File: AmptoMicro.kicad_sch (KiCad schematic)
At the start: 12 parts, among them U1 ADG1207YCPZ-REEL7, U10 ADG1207YCPZ-REEL7, U11 MSP430F6768IPEU, U12 ADL5308ACCZ, U3 ADG1207YCPZ-REEL7, U4 ADG1207YCPZ-REEL7, U5 ADG1207YCPZ-REEL7, U6 ADG1207YCPZ-REEL7, U7 ADG1207YCPZ-REEL7, U8 ADG1207YCPZ-REEL7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

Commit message: With new TMUX
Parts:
- removed U1, U10, U3, U4, U5, U6, U7, U8, U9: ADG1207YCPZ-REEL7, CP_32_2_ADI, symbol ADG_new:ADG1207YCPZ-REEL7
- added U1, U10, U13, U2, U3, U4, U5, U6, U7, U8, U9: TMUX1109PWR, PW_16_TEX, symbol TMUX1109:TMUX1109PWR
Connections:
- net DA1: now also U1.8 (DA), U9.4 (S1A)
- net DA2: now also U2.8 (DA), U9.5 (S2A)
- net DA3: now also U3.8 (DA), U9.6 (S3A)
- net DA4: now also U4.8 (DA), U9.7 (S4A)
- net DA5: now also U13.4 (S1A), U5.8 (DA)
- net DA6: now also U13.5 (S2A), U6.8 (DA)
- net DA7: now also U13.6 (S3A), U7.8 (DA)
- net DA8: now also U13.7 (S4A), U8.8 (DA)
- net DF: now reaches U12.2 (INP)
- net DF: now also U10.8 (DA)
- new net DAA1: U10.4 (S1A), U9.8 (DA)
- new net DAA2: U10.5 (S2A), U13.8 (DA)
- new net DB1: U1.9 (DB), U9.13 (S1B)
- new net DB2: U2.9 (DB), U9.12 (S2B)
- new net DB3: U3.9 (DB), U9.11 (S3B)
- new net DB4: U4.9 (DB), U9.10 (S4B)
- new net DB5: U13.13 (S1B), U5.9 (DB)
- new net DB6: U13.12 (S2B), U6.9 (DB)
- new net DB7: U13.11 (S3B), U7.9 (DB)
- new net DB8: U13.10 (S4B), U8.9 (DB)
- new net DBB1: U10.6 (S3A), U9.9 (DB)
- new net DBB2: U10.7 (S4A), U13.9 (DB)
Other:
- moved on the sheet: DS1, U11A, U11B, U12

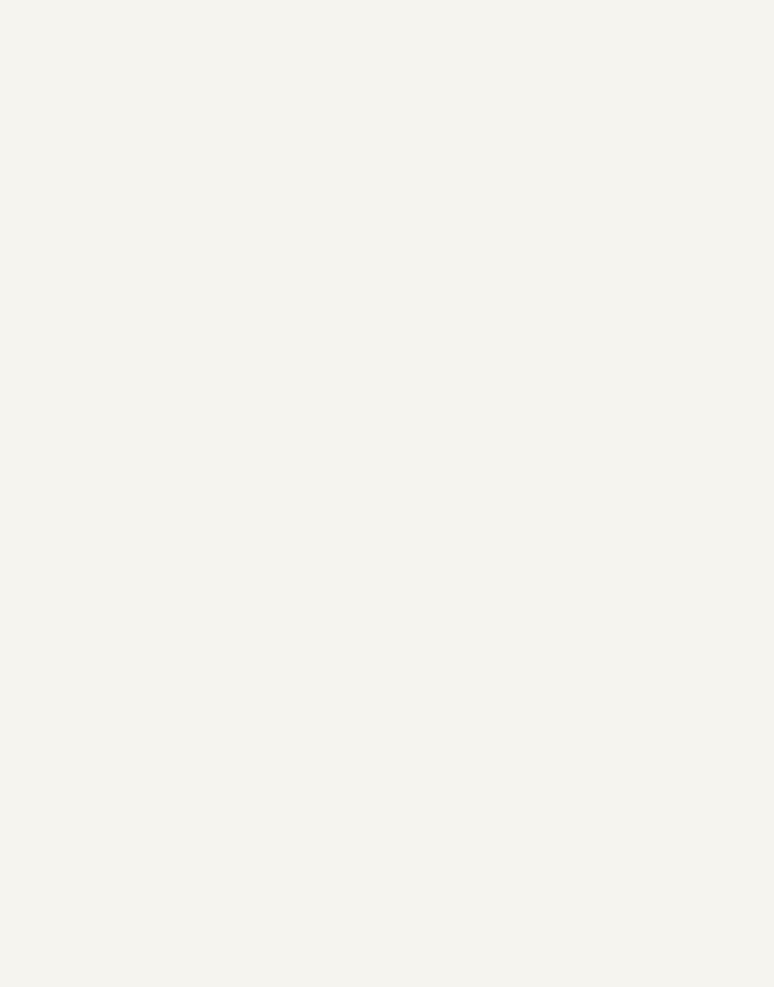
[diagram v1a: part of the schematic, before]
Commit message: Added PLCC 84 socket
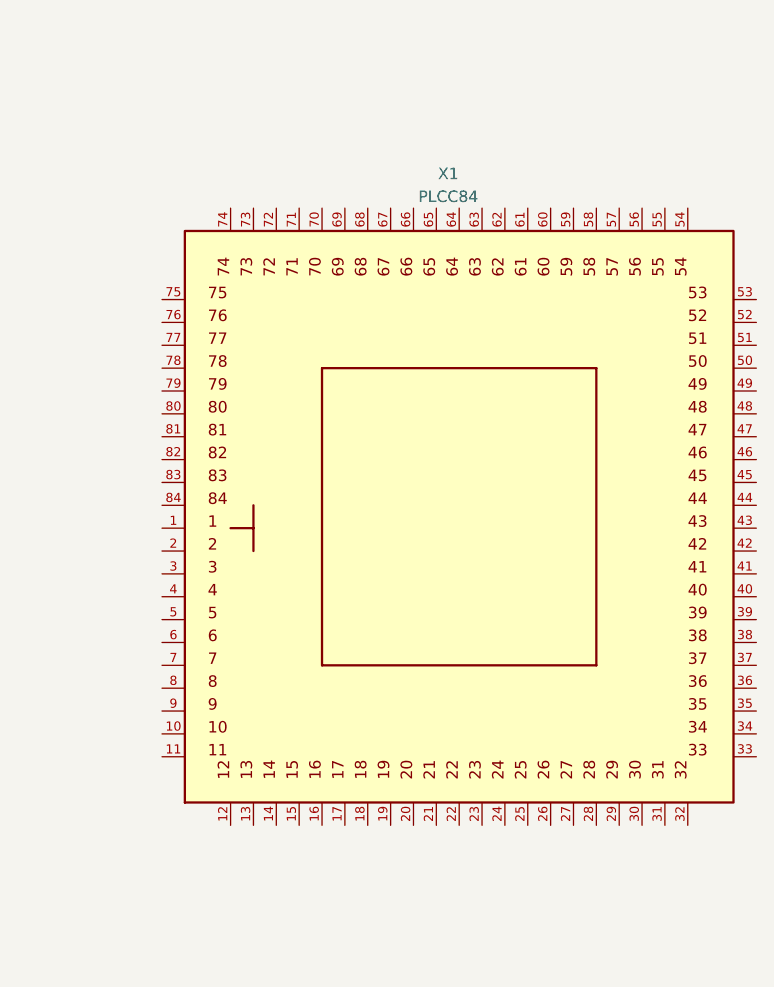
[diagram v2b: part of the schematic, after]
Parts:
- added X1: PLCC84, PLCC84:PLCC84SOCK, symbol PLCC84:PLCC84
